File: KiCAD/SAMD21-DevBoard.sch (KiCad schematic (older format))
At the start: 2 parts

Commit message: Broke out pins from MCU and added data bus protection diode
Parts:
- added C10, C11, C9: .1uF, symbol C_Small
- added C7, C8: 15pF, symbol C_Small
- added C?: C_Small, symbol C_Small
- added L1: 30Ohm - FB, symbol L_Small
- added R2: 10k, symbol R
- added SW1: RESET, symbol SW_Push
- added Y1: 32.768KHz, symbol Crystal_Small
- gave numbers to parts that had none: 2
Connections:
- net labels added: +3.3V, GND, PA10, PA11, PA12, PA13, PA14, PA15, PA16, PA17, PA18, PA19, PA2, PA20, PA21, PA22, PA23, PA27, PA28, PA3, PA30, PA31, PA4, PA5, PA6, PA7, PA8, PA9, PB10, PB11, PB2, PB22, PB23, PB3, PB8, PB9, RESETN, USB_D+, USB_D-, VBUS
- wire segments 0 -> 77
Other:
- moved on the sheet: D101

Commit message: Editing capacitor values, prepping for layout phase
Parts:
- removed SW1: RESET, symbol SW_Push
- added J1, J2: .1\" Headers, symbol Conn_01x20
- added J3: Cortex_Debug, symbol Cortex_Debug
- added SW1: B3FS-4005P, symbol B3FS-4005P
- C12: renamed from C?; value C_Small -> .1uF
- renumbered U101 to U1
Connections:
- net labels added: +5V, RX_LED, SWCLK, SWDIO, TX_LED, VIN
- net labels removed: PA27, PA30, PA31, PB3
- wire segments 77 -> 134
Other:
- note added: "0.100" Headers\n"
- note added: "SWD Debug Header"
- moved on the sheet: C10, C11, C12, C7, C8, C9, D101, L1, R2, U1, Y1

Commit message: Add TX & RX LEDs, tweak values
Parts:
- added C13: 10uF, symbol C_Small
- added D1: YELLOW, symbol LED
- added D2: GREEN, symbol LED
- added R3, R4: 330, symbol R
- C7, C8: value 15pF -> 6.8pF
- L1: value 30Ohm - FB -> 470Ohm - FB
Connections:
- net +3V3: now also C13.2
- net +5V: now also R3.1, R4.1
- net RX_LED: now also D1.1 (K)
- net TX_LED: now also D2.1 (K)
- net at C12.1, L1.2, U1.6: now also C13.1
- new net: D1.2 (A), R3.2
- new net: D2.2 (A), R4.2
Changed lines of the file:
@@
 P 3150 1500
 F 0 "C7" H 3160 1570 50  0000 L CNN
-F 1 "15pF" H 2950 1400 50  0000 L CNN
+F 1 "6.8pF" H 2950 1400 50  0000 L CNN
 F 2 "" H 3150 1500 50  0001 C CNN
 F 3 "" H 3150 1500 50  0001 C CNN
@@
 P 3350 1500
 F 0 "C8" H 3360 1570 50  0000 L CNN
-F 1 "15pF" H 3400 1400 50  0000 L CNN
+F 1 "6.8pF" H 3400 1400 50  0000 L CNN
 F 2 "" H 3350 1500 50  0001 C CNN
 F 3 "" H 3350 1500 50  0001 C CNN
@@
 P 2600 2250
 F 0 "L1" H 2630 2290 50  0000 L CNN
-F 1 "30Ohm - FB" V 2500 2100 28  0000 L CNN
+F 1 "470Ohm - FB" V 2500 2150 28  0000 L CNN
 F 2 "" H 2600 2250 50  0001 C CNN
 F 3 "" H 2600 2250 50  0001 C CNN
@@
 Text GLabel 6000 7050 2    39   Input ~ 0
 PA16
-Text GLabel 9400 5800 2    39   Input ~ 0
+Text GLabel 9600 5950 2    39   Input ~ 0
 TX_LED
 Text GLabel 6000 6150 2    39   Input ~ 0
@@
 Text GLabel 6000 6250 2    39   Input ~ 0
 PB22
-Text GLabel 8850 5450 2    39   Input ~ 0
+Text GLabel 8950 5950 2    39   Input ~ 0
 RX_LED
 Text GLabel 6000 5950 2    39   Input ~ 0
@@
 	2600 2350 2600 2550
 Wire Wire Line
-	3650 2400 2600 2400
+	2200 2400 3650 2400
 Connection ~ 2600 2400
 Wire Wire Line
@@
 	10450 2300 10450 2250
 Connection ~ 10450 2250
+$Comp
+L C_Small C13
+U 1 1 5C02F14F
+P 2200 2650
+F 0 "C13" H 2210 2720 50  0000 L CNN
+F 1 "10uF" H 2210 2570 50  0000 L CNN
+F 2 "" H 2200 2650 50  0001 C CNN
+F 3 "" H 2200 2650 50  0001 C CNN
+	1    2200 2650
+	1    0    0    -1
+$EndComp
+$Comp
+L GND #PWR?
+U 1 1 5C02F19A
+P 2200 2800
+F 0 "#PWR?" H 2200 2550 50  0001 C CNN
+F 1 "GND" H 2200 2650 50  0000 C CNN
+F 2 "" H 2200 2800 50  0001 C CNN
+F 3 "" H 2200 2800 50  0001 C CNN
+	1    2200 2800
+	1    0    0    -1
+$EndComp
+Wire Wire Line
+	2200 2800 2200 2750
+Wire Wire Line
+	2200 2550 2200 2400
+$Comp
+L LED D1
+U 1 1 5C03F384
+P 8850 5550
+F 0 "D1" H 8850 5650 50  0000 C CNN
+F 1 "YELLOW" H 8900 5450 50  0000 C CNN
+F 2 "" H 8850 5550 50  0001 C CNN
+F 3 "" H 8850 5550 50  0001 C CNN
+	1    8850 5550
+	0    -1   -1   0
+$EndComp
+$Comp
+L +5V #PWR?
+U 1 1 5C03F43E
+P 8850 4900
+F 0 "#PWR?" H 8850 4750 50  0001 C CNN
+F 1 "+5V" H 8850 5040 50  0000 C CNN
+F 2 "" H 8850 4900 50  0001 C CNN
+F 3 "" H 8850 4900 50  0001 C CNN
+	1    8850 4900
+	1    0    0    -1
+$EndComp
+$Comp
+L +5V #PWR?
+U 1 1 5C03F474
+P 9500 4900
+F 0 "#PWR?" H 9500 4750 50  0001 C CNN
+F 1 "+5V" H 9500 5040 50  0000 C CNN
+F 2 "" H 9500 4900 50  0001 C CNN
+F 3 "" H 9500 4900 50  0001 C CNN
+	1    9500 4900
+	1    0    0    -1
+$EndComp
+$Comp
+L LED D2
+U 1 1 5C03F4AA
+P 9500 5550
+F 0 "D2" H 9500 5650 50  0000 C CNN
+F 1 "GREEN" H 9550 5450 50  0000 C CNN
+F 2 "" H 9500 5550 50  0001 C CNN
+F 3 "" H 9500 5550 50  0001 C CNN
+	1    9500 5550
+	0    -1   -1   0
+$EndComp
+Wire Wire Line
+	8950 5950 8850 5950
+$Comp
+L R R3
+U 1 1 5C03F994
+P 8850 5150
+F 0 "R3" V 8930 5150 50  0000 C CNN
+F 1 "330" V 8850 5150 50  0000 C CNN
+F 2 "" V 8780 5150 50  0001 C CNN
+F 3 "" H 8850 5150 50  0001 C CNN
+	1    8850 5150
+	1    0    0    -1
+$EndComp
+$Comp
+L R R4
+U 1 1 5C03FA19
+P 9500 5150
+F 0 "R4" V 9580 5150 50  0000 C CNN
+F 1 "330" V 9500 5150 50  0000 C CNN
+F 2 "" V 9430 5150 50  0001 C CNN
+F 3 "" H 9500 5150 50  0001 C CNN
+	1    9500 5150
+	1    0    0    -1
+$EndComp
+Wire Wire Line
+	8850 5000 8850 4900
+Wire Wire Line
+	9500 5000 9500 4900
+Wire Wire Line
+	8850 5400 8850 5300
+Wire Wire Line
+	8850 5950 8850 5700
+Wire Wire Line
+	9500 5700 9500 5950
+Wire Wire Line
+	9500 5950 9600 5950
+Wire Wire Line
+	9500 5400 9500 5300
 $EndSCHEMATC

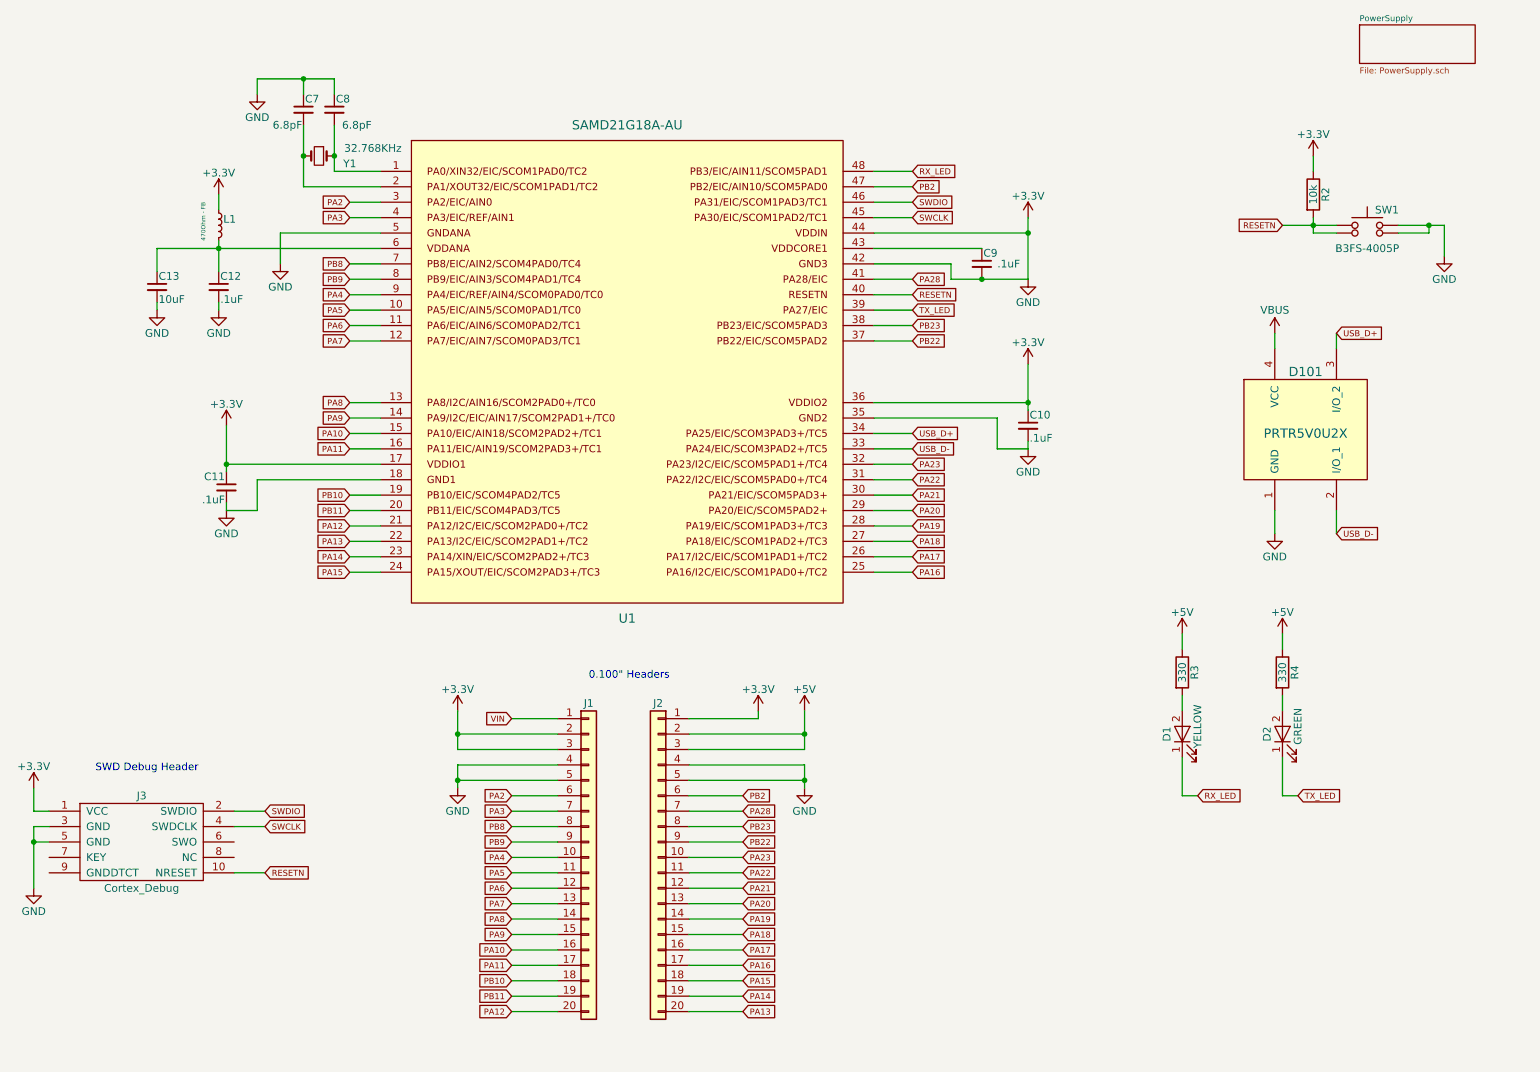
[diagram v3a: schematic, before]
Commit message: Created footprints for switch, micro usb port and crystal
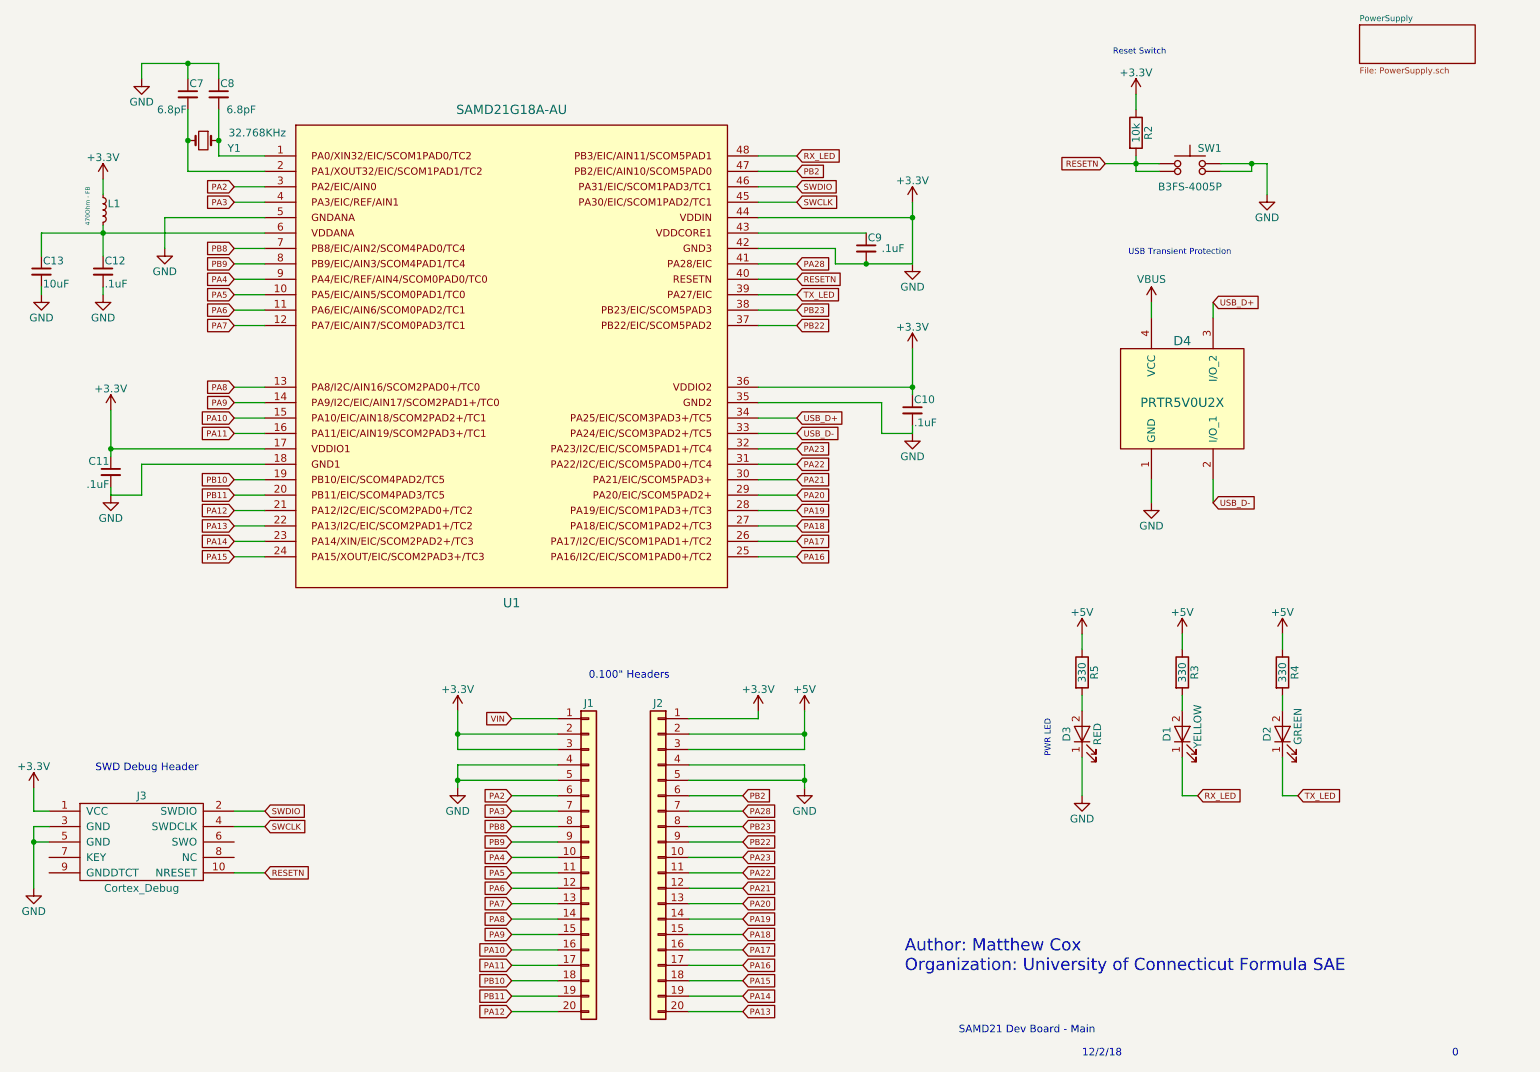
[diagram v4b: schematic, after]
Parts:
- added D3: RED, LEDs:LED_1206, symbol LED
- added R5: 330, Resistors_SMD:R_1210, symbol R
- C10, C11, C12, C13, C9: footprint (none) -> Capacitors_SMD:C_1206
- C7, C8: footprint (none) -> Capacitors_SMD:C_0805
- D1, D2: footprint (none) -> LEDs:LED_1206
- D4: renamed from D101; footprint (none) -> TO_SOT_Packages_SMD:SOT-143
- J1, J2: footprint (none) -> Pin_Headers:Pin_Header_Straight_1x20_Pitch2.54mm
- J3: footprint (none) -> Pin_Headers:Pin_Header_Straight_2x05_Pitch1.27mm
- L1: footprint (none) -> Inductors_SMD:L_1806
- R2, R3, R4: footprint (none) -> Resistors_SMD:R_1210
- SW1: footprint (none) -> B3FS-4:B3FS-4
- U1: footprint (none) -> ATSAMD21G18A-AU:QFP50P900X900X120-48N
- Y1: footprint (none) -> MS1V-T1K:MS1V-T1K
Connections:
- net +3V3: now also D3.1 (K)
- net +5V: now also R5.1
- new net: D3.2 (A), R5.2
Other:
- note added: "0"
- note added: "12/2/18"
- note added: "Author: Matthew Cox\nOrganization: University of Connecticut Formula SAE"
- note added: "PWR LED"
- note added: "Reset Switch"
- note added: "SAMD21 Dev Board - Main"
- note added: "USB Transient Protection"
- moved on the sheet: C10, C11, C12, C13, C7, C8, C9, D4, L1, R2, SW1, U1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

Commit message: Generate netlist and begin layout
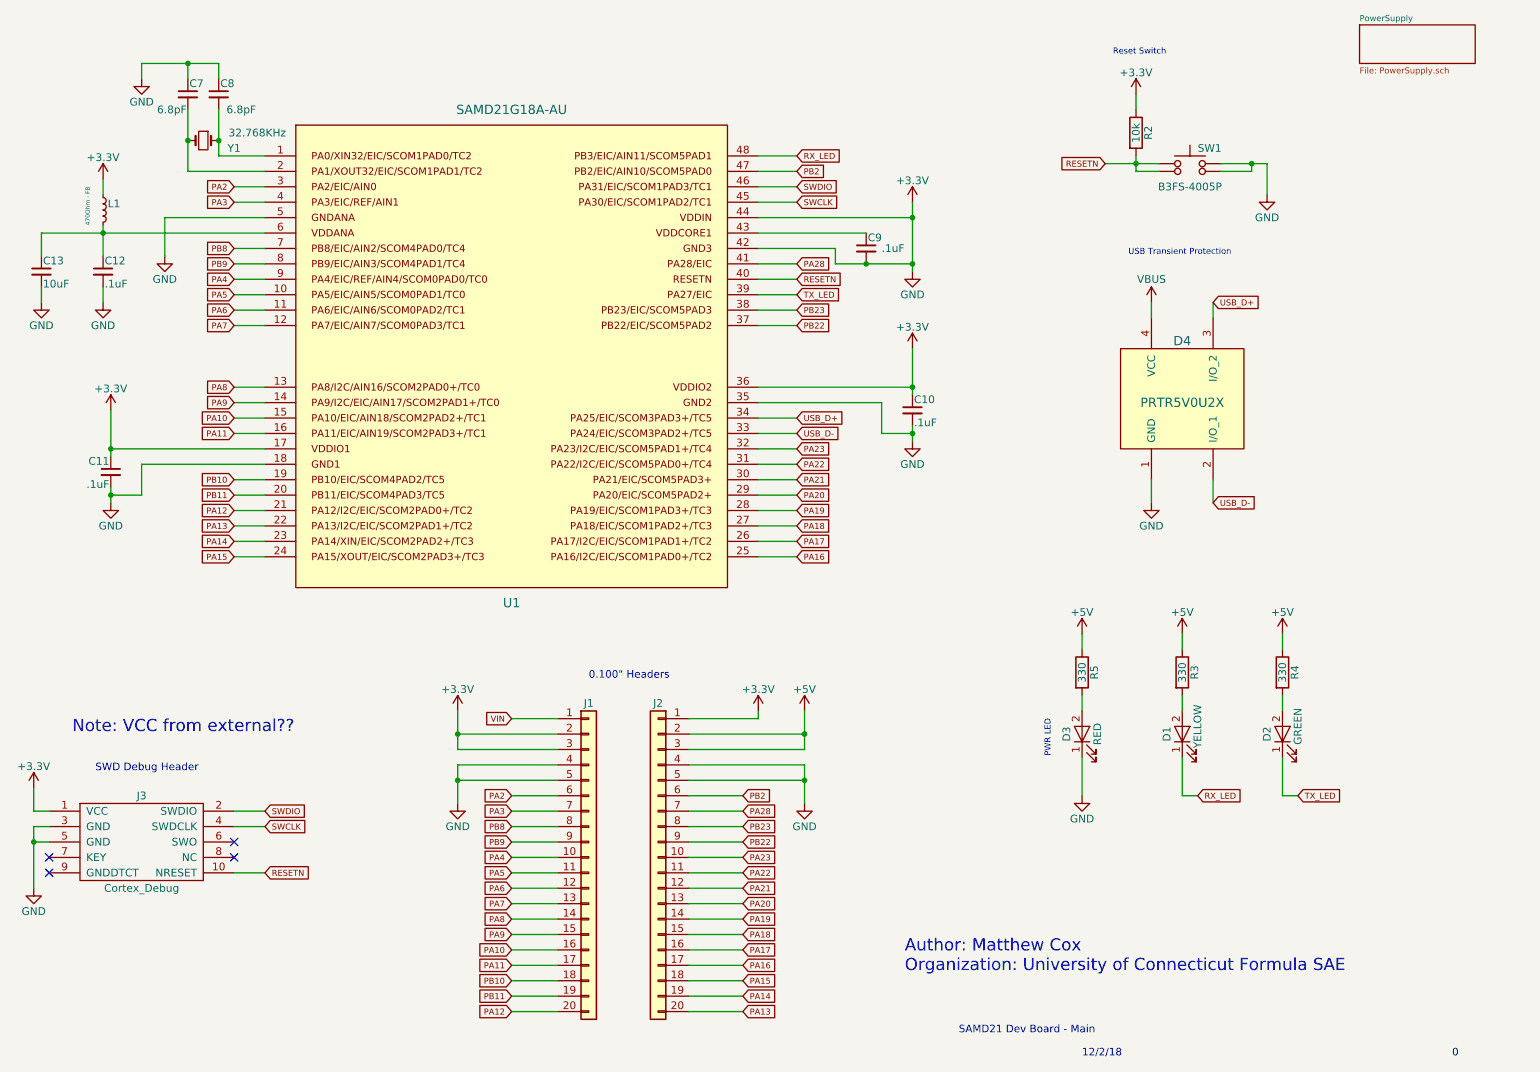
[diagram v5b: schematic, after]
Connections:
- no-connect marks 0 -> 4
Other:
- note added: "Note: VCC from external??"
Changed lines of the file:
@@
 L GND #PWR05
 U 1 1 5BF30FEC
-P 7100 2500
-F 0 "#PWR05" H 7100 2250 50  0001 C CNN
-F 1 "GND" H 7100 2350 50  0000 C CNN
-F 2 "" H 7100 2500 50  0001 C CNN
-F 3 "" H 7100 2500 50  0001 C CNN
-	1    7100 2500
+P 7100 2550
+F 0 "#PWR05" H 7100 2300 50  0001 C CNN
+F 1 "GND" H 7100 2400 50  0000 C CNN
+F 2 "" H 7100 2550 50  0001 C CNN
+F 3 "" H 7100 2550 50  0001 C CNN
+	1    7100 2550
 	1    0    0    -1
 $EndComp
@@
 L GND #PWR07
 U 1 1 5BF3142B
-P 1900 4000
-F 0 "#PWR07" H 1900 3750 50  0001 C CNN
-F 1 "GND" H 1900 3850 50  0000 C CNN
-F 2 "" H 1900 4000 50  0001 C CNN
-F 3 "" H 1900 4000 50  0001 C CNN
-	1    1900 4000
+P 1900 4050
+F 0 "#PWR07" H 1900 3800 50  0001 C CNN
+F 1 "GND" H 1900 3900 50  0000 C CNN
+F 2 "" H 1900 4050 50  0001 C CNN
+F 3 "" H 1900 4050 50  0001 C CNN
+	1    1900 4050
 	-1   0    0    -1
 $EndComp
@@
 L GND #PWR09
 U 1 1 5BF318CB
-P 7100 3600
-F 0 "#PWR09" H 7100 3350 50  0001 C CNN
-F 1 "GND" H 7100 3450 50  0000 C CNN
-F 2 "" H 7100 3600 50  0001 C CNN
-F 3 "" H 7100 3600 50  0001 C CNN
-	1    7100 3600
+P 7100 3650
+F 0 "#PWR09" H 7100 3400 50  0001 C CNN
+F 1 "GND" H 7100 3500 50  0000 C CNN
+F 2 "" H 7100 3650 50  0001 C CNN
+F 3 "" H 7100 3650 50  0001 C CNN
+	1    7100 3650
 	1    0    0    -1
 $EndComp
@@
 L GND #PWR010
 U 1 1 5BF31BBB
-P 1850 2700
-F 0 "#PWR010" H 1850 2450 50  0001 C CNN
-F 1 "GND" H 1850 2550 50  0000 C CNN
-F 2 "" H 1850 2700 50  0001 C CNN
-F 3 "" H 1850 2700 50  0001 C CNN
-	1    1850 2700
+P 1850 2750
+F 0 "#PWR010" H 1850 2500 50  0001 C CNN
+F 1 "GND" H 1850 2600 50  0000 C CNN
+F 2 "" H 1850 2750 50  0001 C CNN
+F 3 "" H 1850 2750 50  0001 C CNN
+	1    1850 2750
 	1    0    0    -1
 $EndComp
@@
 L GND #PWR012
 U 1 1 5BF320EF
-P 2250 2400
-F 0 "#PWR012" H 2250 2150 50  0001 C CNN
-F 1 "GND" H 2250 2250 50  0000 C CNN
-F 2 "" H 2250 2400 50  0001 C CNN
-F 3 "" H 2250 2400 50  0001 C CNN
-	1    2250 2400
+P 2250 2450
+F 0 "#PWR012" H 2250 2200 50  0001 C CNN
+F 1 "GND" H 2250 2300 50  0000 C CNN
+F 2 "" H 2250 2450 50  0001 C CNN
+F 3 "" H 2250 2450 50  0001 C CNN
+	1    2250 2450
 	1    0    0    -1
 $EndComp
@@
 L GND #PWR018
 U 1 1 5BF9D10E
-P 4150 5900
-F 0 "#PWR018" H 4150 5650 50  0001 C CNN
-F 1 "GND" H 4150 5750 50  0000 C CNN
-F 2 "" H 4150 5900 50  0001 C CNN
-F 3 "" H 4150 5900 50  0001 C CNN
-	1    4150 5900
+P 4150 6000
+F 0 "#PWR018" H 4150 5750 50  0001 C CNN
+F 1 "GND" H 4150 5850 50  0000 C CNN
+F 2 "" H 4150 6000 50  0001 C CNN
+F 3 "" H 4150 6000 50  0001 C CNN
+	1    4150 6000
 	1    0    0    -1
 $EndComp
@@
 L GND #PWR020
 U 1 1 5BF9D16A
-P 6400 5900
-F 0 "#PWR020" H 6400 5650 50  0001 C CNN
-F 1 "GND" H 6400 5750 50  0000 C CNN
-F 2 "" H 6400 5900 50  0001 C CNN
-F 3 "" H 6400 5900 50  0001 C CNN
-	1    6400 5900
+P 6400 6000
+F 0 "#PWR020" H 6400 5750 50  0001 C CNN
+F 1 "GND" H 6400 5850 50  0000 C CNN
+F 2 "" H 6400 6000 50  0001 C CNN
+F 3 "" H 6400 6000 50  0001 C CNN
+	1    6400 6000
 	1    0    0    -1
 $EndComp
@@
 	6100 2200 7100 2200
 Wire Wire Line
-	7100 2500 7100 2100
+	7100 2100 7100 2550
 Connection ~ 7100 2200
 Wire Wire Line
@@
 Connection ~ 1900 3700
 Wire Wire Line
-	1900 4000 1900 3950
+	1900 3950 1900 4050
 Wire Wire Line
 	2900 3800 2100 3800
@@
 Connection ~ 7100 3300
 Wire Wire Line
-	7100 3600 7100 3550
+	7100 3550 7100 3650
 Wire Wire Line
 	6100 3400 6900 3400
@@
 Connection ~ 1850 2300
 Wire Wire Line
-	1850 2700 1850 2650
-Wire Wire Line
-	2250 2400 2250 2200
+	1850 2650 1850 2750
+Wire Wire Line
+	2250 2200 2250 2450
 Wire Wire Line
 	2250 2200 2900 2200
@@
 	6100 2600 6350 2600
 Wire Wire Line
-	9400 2050 9400 1850
+	9400 1850 9400 2050
 Wire Wire Line
 	8550 1500 8550 1400
@@
 Wire Wire Line
 	2700 4400 2900 4400
-Wire Wire Line
-	2700 6050 2900 6050
 Wire Wire Line
 	2700 6150 2900 6150
@@
 	6100 5450 6100 5400
 Wire Wire Line
-	6400 5750 6400 5900
+	6400 5750 6400 6000
 Wire Wire Line
 	6400 5750 5650 5750
@@
 Connection ~ 6400 5550
 Wire Wire Line
-	4800 5650 4150 5650
-Wire Wire Line
-	4150 5650 4150 5400
+	4150 5650 4800 5650
+Wire Wire Line
+	4150 5400 4150 5650
 Wire Wire Line
 	4800 5550 4150 5550
 Connection ~ 4150 5550
 Wire Wire Line
-	4150 5900 4150 5750
+	4150 5750 4150 6000
 Wire Wire Line
 	4150 5750 4800 5750
@@
 	8550 1900 8700 1900
 Wire Wire Line
-	9400 1850 9100 1850
+	9100 1850 9400 1850
 Wire Wire Line
 	9100 1900 9300 1900
@@
 L GND #PWR022
 U 1 1 5C02F19A
-P 1450 2700
-F 0 "#PWR022" H 1450 2450 50  0001 C CNN
-F 1 "GND" H 1450 2550 50  0000 C CNN
-F 2 "" H 1450 2700 50  0001 C CNN
-F 3 "" H 1450 2700 50  0001 C CNN
-	1    1450 2700
-	1    0    0    -1
-$EndComp
-Wire Wire Line
-	1450 2700 1450 2650
+P 1450 2750
+F 0 "#PWR022" H 1450 2500 50  0001 C CNN
+F 1 "GND" H 1450 2600 50  0000 C CNN
+F 2 "" H 1450 2750 50  0001 C CNN
+F 3 "" H 1450 2750 50  0001 C CNN
+	1    1450 2750
+	1    0    0    -1
+$EndComp
+Wire Wire Line
+	1450 2650 1450 2750
 Wire Wire Line
 	1450 2450 1450 2300
@@
 Text Notes 7050 7100 0    79   ~ 0
 Author: Matthew Cox\nOrganization: University of Connecticut Formula SAE
+Wire Wire Line
+	2700 6050 2900 6050
+Text Notes 1650 5550 0    79   ~ 0
+Note: VCC from external??
+Connection ~ 7100 3600
+Connection ~ 7100 2500
+Connection ~ 1900 4000
+NoConn ~ 2700 6250
+NoConn ~ 2700 6350
+NoConn ~ 1500 6350
+NoConn ~ 1500 6450
 $EndSCHEMATC
